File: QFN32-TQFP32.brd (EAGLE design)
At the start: 20 x 43.2 mm, 8 parts

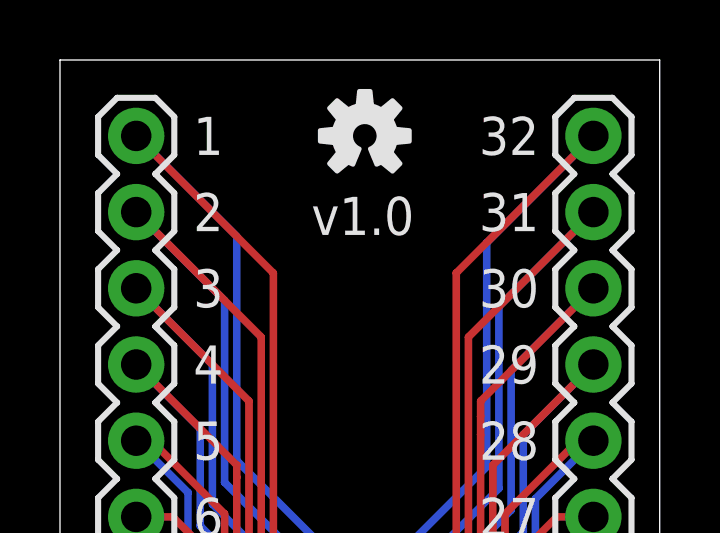
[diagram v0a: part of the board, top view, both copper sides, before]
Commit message: Silk and board revision
Worked several silk screen issues and narrowed some boards.
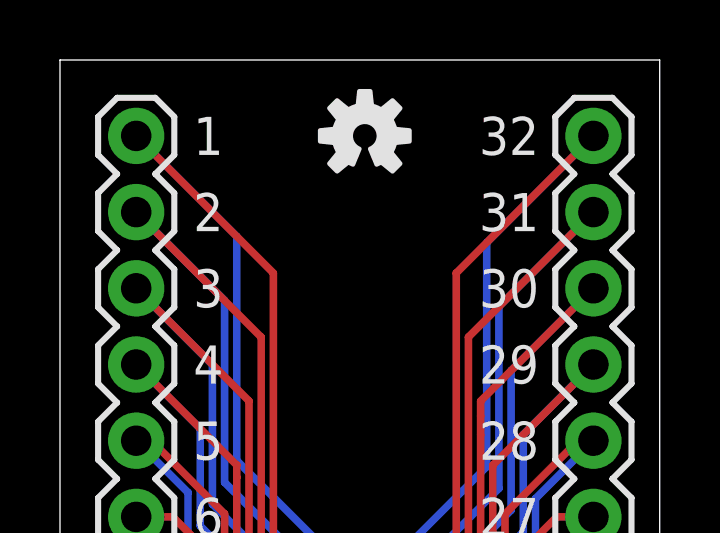
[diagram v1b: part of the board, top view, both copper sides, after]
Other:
- board text removed: "v1.0"
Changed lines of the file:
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@@
 <layer number="23" name="tOrigins" color="15" fill="1" visible="yes" active="yes"/>
 <layer number="24" name="bOrigins" color="15" fill="1" visible="yes" active="yes"/>
-<layer number="25" name="tNames" color="7" fill="1" visible="yes" active="yes"/>
-<layer number="26" name="bNames" color="7" fill="1" visible="yes" active="yes"/>
+<layer number="25" name="tNames" color="7" fill="1" visible="no" active="yes"/>
+<layer number="26" name="bNames" color="7" fill="1" visible="no" active="yes"/>
 <layer number="27" name="tValues" color="7" fill="1" visible="no" active="yes"/>
 <layer number="28" name="bValues" color="7" fill="1" visible="no" active="yes"/>
@@
 <text x="15.875" y="24.765" size="1.27" layer="22" rot="MR0">26</text>
 <text x="29.464" y="-8.128" size="1.778" layer="51">Kevin Neubauer</text>
-<text x="18.542" y="37.338" size="1.27" layer="21">v1.0</text>
 <text x="19.05" y="4.445" size="1.27" layer="21">PAD</text>
 <text x="23.495" y="14.986" size="1.27" layer="21" ratio="15" rot="R180">QFN-32</text>
